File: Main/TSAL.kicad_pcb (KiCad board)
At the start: 2 copper layers, 140 x 70 mm, 156 parts, among them J1 Micro-Fit, J2 Mini-SPOX, J3 Mini-SPOX, J4 Mini-SPOX, J5 Mini-SPOX, Q1 IRLML2502, Q10 NPN, Q11 MJD122, Q12 PNP, Q2 IRLML2502, Q3 IRLML2502, Q4 IRLML2502, Q5 IRLML2502, Q6 BSC0904NSI, Q7 BSC0902NSI, Q8 BSC0902NSI, Q9 MJD122, U1 74HC08, U10 TLV431, U11 TLV431, U2 74HC08, U3 LMC555, U4 TPS562200, U5 TPS63020, U6 MAX40200AUK, U7 INA180A3, U8 TLV9104, U9 LM25117

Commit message: Main: archive symbols and footprints
Kicad library management is really terrible.
This is pulled together with janky scripts and sed.
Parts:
- C1, C15, C16, C17, C2, C20, C21, C25, C26, C27, C28, C3, C34, C37, C38, C39, C4, C40, C41, C42, C43, C6: footprint Capacitor_SMD:C_0402_1005Metric -> archive:C_0402_1005Metric
- C10, C11, C12, C13, C14, C5, C9: footprint Capacitor_SMD:C_0805_2012Metric -> archive:C_0805_2012Metric
- C18, C19: footprint Capacitor_SMD:CP_Elec_8x10.5 -> archive:CP_Elec_8x10.5
- C22, C23, C24, C29, C30, C31, C7, C8: footprint Capacitor_SMD:C_1210_3225Metric -> archive:C_1210_3225Metric
- C32, C33, C35, C36: footprint Capacitor_THT:CP_Radial_D30.0mm_P10.00mm_SnapIn -> archive:CP_Radial_D30.0mm_P10.00mm_SnapIn
- D1, D2: footprint Diode_SMD:D_SOD-123 -> archive:D_SOD-123
- D3: footprint Diode_SMD:D_SOD-323 -> archive:D_SOD-323
- F1, F2: footprint Fuse:Fuseholder_Littelfuse_Nano2_154x -> archive:Fuseholder_Littelfuse_Nano2_154x
- H1, H2, H3, H4: footprint MountingHole:MountingHole_3.2mm_M3_Pad -> archive:MountingHole_3.2mm_M3_Pad
- J1: footprint Connector_Molex:Molex_Micro-Fit_3.0_43045-0412_2x02_P3.00mm_Vertical -> archive:Molex_Micro-Fit_3.0_43045-0412_2x02_P3.00mm_Vertical
- J2: footprint Connector_Molex:Molex_SPOX_5267-03A_1x03_P2.50mm_Vertical -> archive:Molex_SPOX_5267-03A_1x03_P2.50mm_Vertical
- J3: footprint Connector_Molex:Molex_SPOX_5267-04A_1x04_P2.50mm_Vertical -> archive:Molex_SPOX_5267-04A_1x04_P2.50mm_Vertical
- J4: footprint Connector_Molex:Molex_SPOX_5267-06A_1x06_P2.50mm_Vertical -> archive:Molex_SPOX_5267-06A_1x06_P2.50mm_Vertical
- J5: footprint Connector_Molex:Molex_SPOX_5267-02A_1x02_P2.50mm_Vertical -> archive:Molex_SPOX_5267-02A_1x02_P2.50mm_Vertical
- JP1, R1, R10, R11, R13, R14, R19, R2, R20, R21, R22, R23, R24, R25, R26, R27, R30, R31, R33, R34, R36, R37, R38, R39, R4, R40, R41, R42, R43, R44, R45, R47, R48, R49, R50, R6, R7, R8, R9: footprint Resistor_SMD:R_0402_1005Metric -> archive:R_0402_1005Metric
- L1, L2: footprint Inductor_SMD:L_Bourns-SRN4018 -> archive:L_Bourns-SRN4018
- L3: footprint Inductor_SMD:L_Bourns-SRN8040_8x8.15mm -> archive:L_Bourns-SRN8040_8x8.15mm
- L4: footprint Inductor_SMD:L_Bourns_SRP1245A -> archive:L_Bourns_SRP1245A
- Q1, Q10, Q12, Q2, Q3, Q4, Q5, U10, U11: footprint Package_TO_SOT_SMD:SOT-23 -> archive:SOT-23
- Q11, Q9: footprint Package_TO_SOT_SMD:TO-252-2 -> archive:TO-252-2
- Q6, Q7, Q8: footprint Package_TO_SOT_SMD:TDSON-8-1 -> archive:TDSON-8-1
- R12, R32: footprint Resistor_SMD:R_2512_6332Metric -> archive:R_2512_6332Metric
- R15, R16, R17, R18, R28, R29, R3, R35, R46, R5, R51: footprint Resistor_SMD:R_0805_2012Metric -> archive:R_0805_2012Metric
- TP1, TP10, TP11, TP2, TP3, TP4, TP5, TP6, TP7, TP8, TP9: footprint TestPoint:TestPoint_Loop_D2.50mm_Drill1.0mm -> archive:TestPoint_Loop_D2.50mm_Drill1.0mm
- U1, U2, U8: footprint Package_SO:TSSOP-14_4.4x5mm_P0.65mm -> archive:TSSOP-14_4.4x5mm_P0.65mm
- U3: footprint Package_SO:TSSOP-8_3x3mm_P0.65mm -> archive:TSSOP-8_3x3mm_P0.65mm
- U4: footprint Package_TO_SOT_SMD:SOT-23-6 -> archive:SOT-23-6
- U5: footprint project:TPS63020 -> archive:TPS63020
- U6, U7: footprint Package_TO_SOT_SMD:SOT-23-5 -> archive:SOT-23-5
- U9: footprint Package_SO:ETSSOP-20-1EP_4.4x6.5mm_P0.65mm_EP3x4.2mm -> archive:ETSSOP-20-1EP_4.4x6.5mm_P0.65mm_EP3x4.2mm
- ZZ1, ZZ2, ZZ3, ZZ4, ZZ5, ZZ6, ZZ7, ZZ8: footprint project:Trace_0.2mmx0.6mm -> archive:Trace_0.2mmx0.6mm

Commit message: Main board rev b release?
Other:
- rule pad_to_mask_clearance: 0.051 -> 0

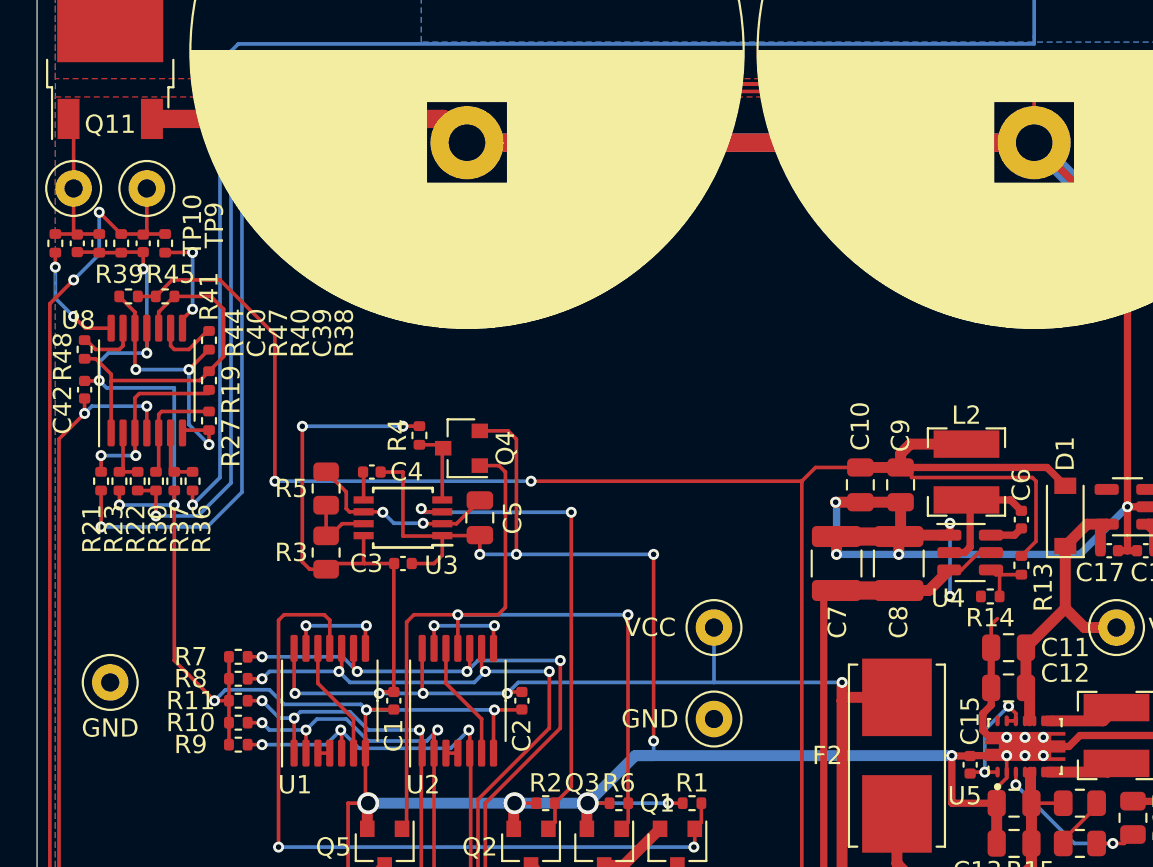
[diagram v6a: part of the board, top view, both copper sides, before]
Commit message: kicad please I wanted solid gnd connections
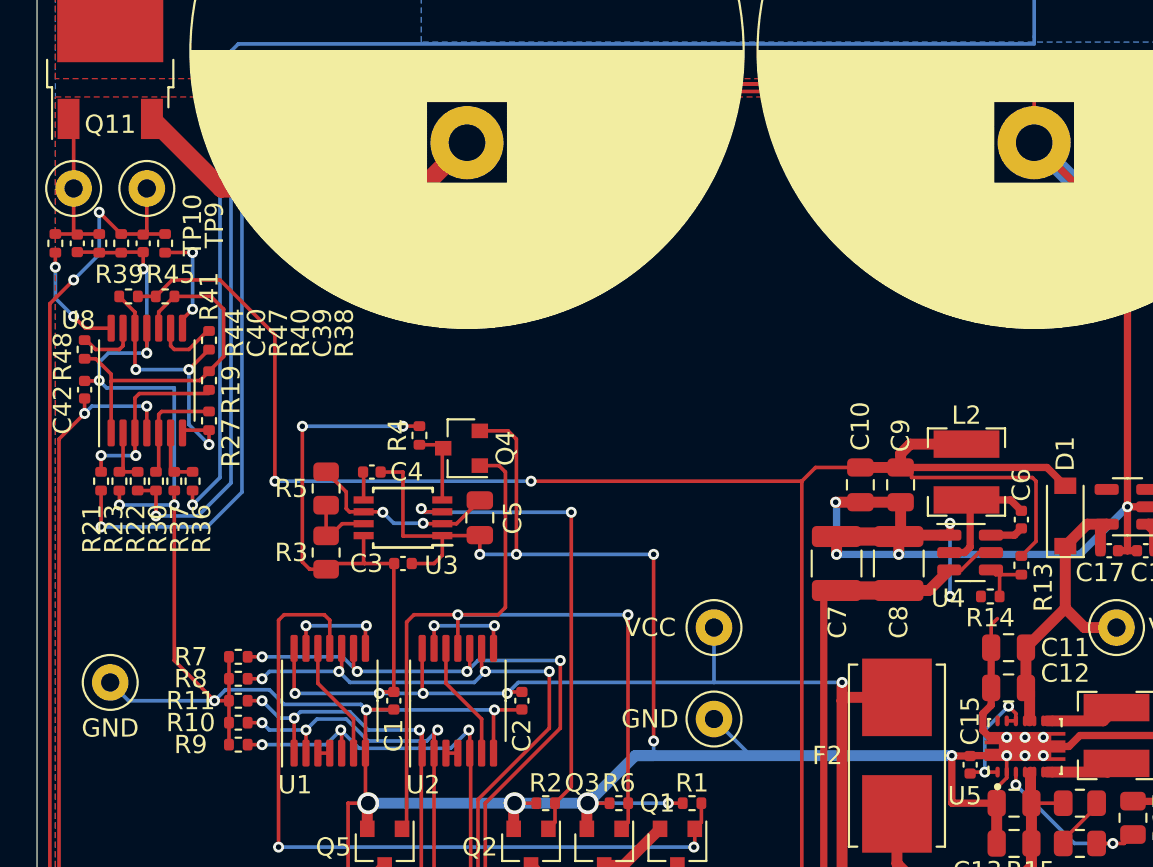
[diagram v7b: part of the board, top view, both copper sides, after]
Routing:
- net GND: track 637.6 -> 597.6 mm
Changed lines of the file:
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@@
     (thickness 1.6)
     (drawings 26)
-    (tracks 1189)
+    (tracks 1192)
     (zones 0)
     (modules 156)
@@
   )
   (setup
-    (last_trace_width 0.2)
+    (last_trace_width 0.4)
     (user_trace_width 0.4)
     (user_trace_width 0.6)
@@
     (mod_text_size 1 1)
     (mod_text_width 0.15)
-    (pad_size 0.2 0.2)
-    (pad_drill 0)
+    (pad_size 4 4)
+    (pad_drill 2)
     (pad_to_mask_clearance 0)
     (aux_axis_origin 70 70)
@@
     )
     (pad 2 thru_hole circle (at 10 0 90) (size 4 4) (drill 2) (layers *.Cu *.Mask)
-      (net 38 /Power/VCAP1))
+      (net 38 /Power/VCAP1) (zone_connect 2))
     (pad 1 thru_hole rect (at 0 0 90) (size 4 4) (drill 2) (layers *.Cu *.Mask)
-      (net 30 /Power/VCAP2))
+      (net 30 /Power/VCAP2) (zone_connect 2))
     (model ${KISYS3DMOD}/Capacitor_THT.3dshapes/CP_Radial_D30.0mm_P10.00mm_SnapIn.wrl
       (at (xyz 0 0 0))
@@
     )
     (pad 2 thru_hole circle (at 10 0 90) (size 4 4) (drill 2) (layers *.Cu *.Mask)
-      (net 38 /Power/VCAP1))
+      (net 38 /Power/VCAP1) (zone_connect 2))
     (pad 1 thru_hole rect (at 0 0 90) (size 4 4) (drill 2) (layers *.Cu *.Mask)
-      (net 30 /Power/VCAP2))
+      (net 30 /Power/VCAP2) (zone_connect 2))
     (model ${KISYS3DMOD}/Capacitor_THT.3dshapes/CP_Radial_D30.0mm_P10.00mm_SnapIn.wrl
       (at (xyz 0 0 0))
@@
     (descr "Molex Micro-Fit 3.0 Connector System, 43045-0412 (compatible alternatives: 43045-0413, 43045-0424), 2 Pins per row (http://www.molex.com/pdm_docs/sd/430450212_sd.pdf), generated with kicad-footprint-generator")
     (tags "connector Molex Micro-Fit_3.0 side entry")
+    (zone_connect 2)
     (fp_text reference J1 (at -2.7 -3.3) (layer F.SilkS)
       (effects (font (size 1 1) (thickness 0.15)))
@@
     )
     (pad 4 thru_hole circle (at 3 3) (size 1.5 1.5) (drill 1) (layers *.Cu *.Mask)
-      (net 6 VIN))
+      (net 6 VIN) (zone_connect 2))
     (pad 3 thru_hole circle (at 0 3) (size 1.5 1.5) (drill 1) (layers *.Cu *.Mask)
-      (net 1 GND))
+      (net 1 GND) (zone_connect 2))
     (pad 2 thru_hole circle (at 3 0) (size 1.5 1.5) (drill 1) (layers *.Cu *.Mask)
-      (net 6 VIN))
+      (net 6 VIN) (zone_connect 2))
     (pad 1 thru_hole roundrect (at 0 0) (size 1.5 1.5) (drill 1) (layers *.Cu *.Mask) (roundrect_rratio 0.1666666666666667)
-      (net 1 GND))
-    (pad "" np_thru_hole circle (at 6 3.94) (size 1 1) (drill 1) (layers *.Cu *.Mask))
-    (pad "" np_thru_hole circle (at -3 3.94) (size 1 1) (drill 1) (layers *.Cu *.Mask))
+      (net 1 GND) (zone_connect 2))
+    (pad "" np_thru_hole circle (at 6 3.94) (size 1 1) (drill 1) (layers *.Cu *.Mask)
+      (zone_connect 2))
+    (pad "" np_thru_hole circle (at -3 3.94) (size 1 1) (drill 1) (layers *.Cu *.Mask)
+      (zone_connect 2))
     (model ${KISYS3DMOD}/Connector_Molex.3dshapes/Molex_Micro-Fit_3.0_43045-0412_2x02_P3.00mm_Vertical.wrl
       (at (xyz 0 0 0))
@@
     (descr "TO-252 / DPAK SMD package, http://www.infineon.com/cms/en/product/packages/PG-TO252/PG-TO252-3-1/")
     (tags "DPAK TO-252 DPAK-3 TO-252-3 SOT-428")
+    (zone_connect 2)
     (attr smd)
     (fp_text reference Q11 (at -4.5 0) (layer F.SilkS)
@@
       (effects (font (size 1 1) (thickness 0.15)))
     )
-    (pad "" smd rect (at 0.425 1.525 90) (size 3.05 2.75) (layers F.Paste))
-    (pad "" smd rect (at 3.775 -1.525 90) (size 3.05 2.75) (layers F.Paste))
-    (pad "" smd rect (at 0.425 -1.525 90) (size 3.05 2.75) (layers F.Paste))
-    (pad "" smd rect (at 3.775 1.525 90) (size 3.05 2.75) (layers F.Paste))
+    (pad "" smd rect (at 0.425 1.525 90) (size 3.05 2.75) (layers F.Paste)
+      (zone_connect 2))
+    (pad "" smd rect (at 3.775 -1.525 90) (size 3.05 2.75) (layers F.Paste)
+      (zone_connect 2))
+    (pad "" smd rect (at 0.425 -1.525 90) (size 3.05 2.75) (layers F.Paste)
+      (zone_connect 2))
+    (pad "" smd rect (at 3.775 1.525 90) (size 3.05 2.75) (layers F.Paste)
+      (zone_connect 2))
     (pad 2 smd rect (at 2.1 0 90) (size 6.4 5.8) (layers F.Cu F.Mask)
-      (net 38 /Power/VCAP1))
+      (net 38 /Power/VCAP1) (zone_connect 2))
     (pad 3 smd rect (at -4.2 2.28 90) (size 2.2 1.2) (layers F.Cu F.Paste F.Mask)
-      (net 1 GND))
+      (net 1 GND) (zone_connect 2))
     (pad 1 smd rect (at -4.2 -2.28 90) (size 2.2 1.2) (layers F.Cu F.Paste F.Mask)
-      (net 41 /Power/BAL_CTRL1))
+      (net 41 /Power/BAL_CTRL1) (zone_connect 2))
     (model ${KISYS3DMOD}/Package_TO_SOT_SMD.3dshapes/TO-252-2.wrl
       (at (xyz 0 0 0))
@@
     (descr "CP, Radial series, Radial, pin pitch=10.00mm, , diameter=30mm, Electrolytic Capacitor, , http://www.vishay.com/docs/28342/058059pll-si.pdf")
     (tags "CP Radial series Radial pin pitch 10.00mm  diameter 30mm Electrolytic Capacitor")
+    (zone_connect 1)
     (fp_text reference C36 (at -5.5 -13 180) (layer F.SilkS)
       (effects (font (size 1 1) (thickness 0.15)))
@@
     )
     (pad 2 thru_hole circle (at 10 0 270) (size 4 4) (drill 2) (layers *.Cu *.Mask)
-      (net 1 GND))
+      (net 1 GND) (zone_connect 1) (thermal_width 1) (thermal_gap 0.4))
     (pad 1 thru_hole rect (at 0 0 270) (size 4 4) (drill 2) (layers *.Cu *.Mask)
-      (net 38 /Power/VCAP1))
+      (net 38 /Power/VCAP1) (zone_connect 2))
     (model ${KISYS3DMOD}/Capacitor_THT.3dshapes/CP_Radial_D30.0mm_P10.00mm_SnapIn.wrl
       (at (xyz 0 0 0))
@@
     (descr "CP, Radial series, Radial, pin pitch=10.00mm, , diameter=30mm, Electrolytic Capacitor, , http://www.vishay.com/docs/28342/058059pll-si.pdf")
     (tags "CP Radial series Radial pin pitch 10.00mm  diameter 30mm Electrolytic Capacitor")
+    (zone_connect 1)
     (fp_text reference C35 (at -5.5 13 180) (layer F.SilkS)
       (effects (font (size 1 1) (thickness 0.15)))
@@
     )
     (pad 2 thru_hole circle (at 10 0 270) (size 4 4) (drill 2) (layers *.Cu *.Mask)
-      (net 1 GND))
+      (net 1 GND) (zone_connect 1) (thermal_width 1) (thermal_gap 0.4))
     (pad 1 thru_hole rect (at 0 0 270) (size 4 4) (drill 2) (layers *.Cu *.Mask)
-      (net 38 /Power/VCAP1))
+      (net 38 /Power/VCAP1) (zone_connect 2))
     (model ${KISYS3DMOD}/Capacitor_THT.3dshapes/CP_Radial_D30.0mm_P10.00mm_SnapIn.wrl
       (at (xyz 0 0 0))
@@
     )
     (pad 1 thru_hole circle (at 0 0) (size 2 2) (drill 1) (layers *.Cu *.Mask)
-      (net 38 /Power/VCAP1))
+      (net 38 /Power/VCAP1) (zone_connect 2))
     (model ${KISYS3DMOD}/TestPoint.3dshapes/TestPoint_Loop_D2.50mm_Drill1.0mm.wrl
       (at (xyz 0 0 0))
@@
   (segment (start 186.4 126.4) (end 186 126) (width 0.2) (layer F.Cu) (net 1) (status 30))
   (segment (start 186.4 127.4) (end 186.4 126.4) (width 0.2) (layer F.Cu) (net 1) (status 30))
-  (segment (start 196 131.5) (end 197.5 133) (width 0.6) (layer F.Cu) (net 1) (status 20))
-  (segment (start 196 127) (end 196 131.5) (width 0.6) (layer F.Cu) (net 1) (status 10))
   (via (at 171 101) (size 0.6) (drill 0.3) (layers F.Cu B.Cu) (net 1))
   (via (at 173 101) (size 0.6) (drill 0.3) (layers F.Cu B.Cu) (net 1))
@@
   (segment (start 129.6 95.6) (end 124.5 90.5) (width 0.4) (layer F.Cu) (net 1) (status 20))
   (segment (start 129.6 110.4) (end 129.6 95.6) (width 0.4) (layer F.Cu) (net 1))
-  (segment (start 92.2 89.2) (end 93.5 90.5) (width 1) (layer F.Cu) (net 1) (status 30))
-  (segment (start 76.28 89.2) (end 92.2 89.2) (width 1) (layer F.Cu) (net 1) (status 30))
-  (segment (start 93.5 90.5) (end 124.5 90.5) (width 1) (layer F.Cu) (net 1) (status 30))
   (segment (start 137 103) (end 124.5 90.5) (width 1) (layer B.Cu) (net 1) (status 20))
   (segment (start 171 103) (end 137 103) (width 1) (layer B.Cu) (net 1))
@@
   (segment (start 196 104.6) (end 200 100.6) (width 1) (layer B.Cu) (net 1))
   (segment (start 196 124) (end 196 104.6) (width 1) (layer B.Cu) (net 1) (status 10))
-  (segment (start 93.5 90.5) (end 124.5 90.5) (width 1) (layer B.Cu) (net 1) (status 30))
   (segment (start 196 124) (end 196 127) (width 1) (layer F.Cu) (net 1) (status 30))
   (via (at 124 123) (size 0.6) (drill 0.3) (layers F.Cu B.Cu) (net 1) (status 30))
@@
   (segment (start 128.9 137.6) (end 110.6 137.6) (width 0.2) (layer F.Cu) (net 1))
   (segment (start 130.5 136) (end 128.9 137.6) (width 0.2) (layer F.Cu) (net 1))
+  (segment (start 109 124) (end 107 122) (width 0.2) (layer B.Cu) (net 1))
+  (segment (start 120 124) (end 109 124) (width 0.2) (layer B.Cu) (net 1))
+  (segment (start 74.999999 120.999999) (end 74 120) (width 0.2) (layer B.Cu) (net 1))
+  (segment (start 79.7 121) (end 74.999999 120.999999) (width 0.2) (layer B.Cu) (net 1))
+  (segment (start 196 127) (end 196 131.5) (width 0.6) (layer F.Cu) (net 1) (status 10))
+  (segment (start 196 131.5) (end 197.5 133) (width 0.6) (layer F.Cu) (net 1) (status 20))
+  (segment (start 91 93) (end 93.5 90.5) (width 1) (layer F.Cu) (net 1))
+  (segment (start 80.08 93) (end 91 93) (width 1) (layer F.Cu) (net 1))
+  (segment (start 76.28 89.2) (end 80.08 93) (width 1) (layer F.Cu) (net 1))
   (via (at 114 120) (size 0.6) (drill 0.3) (layers F.Cu B.Cu) (net 2))
   (segment (start 117 120.815) (end 114.185 120.815) (width 0.6) (layer F.Cu) (net 2) (status 10))

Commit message: increase output filter capacitor value
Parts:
- C10, C11, C12, C13, C14, C9: value 10uF -> 22uF
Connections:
- U5 pad 14: (no net) -> Net-(U5-Pad14)
- U6 pad 4: (no net) -> Net-(U6-Pad4)
- U9 pad 7: (no net) -> Net-(U9-Pad7)
